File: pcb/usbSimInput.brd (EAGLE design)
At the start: 65.7 x 63.5 mm, 24 parts, among them U1 MEGA16-P, X1 12MHz

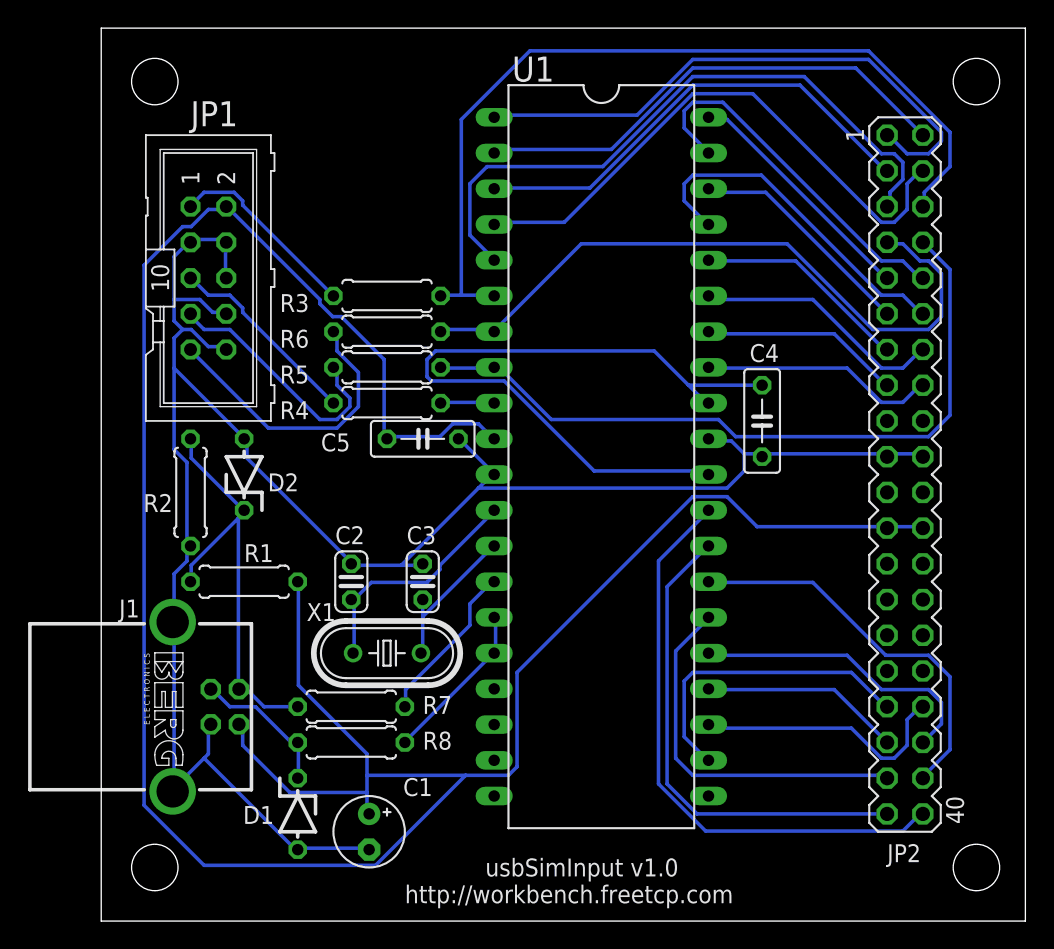
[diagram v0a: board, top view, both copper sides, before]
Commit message: Layout tweaks for Seeed DRU
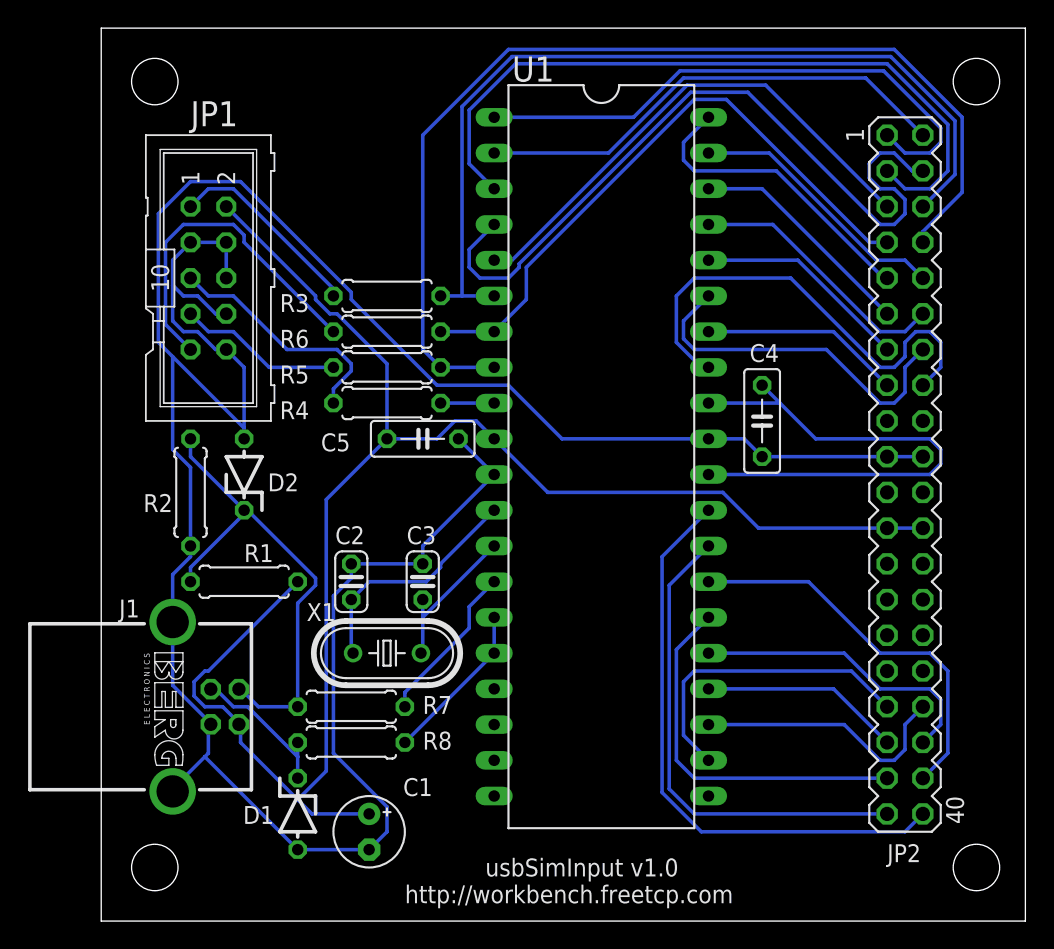
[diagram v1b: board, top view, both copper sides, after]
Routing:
- net VCC: track 186.6 -> 119.6 mm
- net GND: track 148.7 -> 197.6 mm
- net PB7: track 52.3 -> 73.8 mm
- net PB2: track 33.5 -> 52.2 mm
- net PA7: track 16.8 -> 33.8 mm
- net PB3: track 40.7 -> 54.8 mm
- net N$7: track 51.2 -> 37.5 mm
- net PB4: track 46.3 -> 36.7 mm
- net PA5: track 18.0 -> 25.3 mm
- net PA1: track 26.1 -> 18.9 mm
- net N$3: track 18.3 -> 11.7 mm
- net PA3: track 24.9 -> 18.9 mm
- net PB6: track 49.0 -> 44.1 mm
- net USB-: track 30.4 -> 34.7 mm
- net PA0: track 17.5 -> 21.7 mm
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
